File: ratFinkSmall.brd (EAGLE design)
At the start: 82.2 x 80 mm, 30 parts

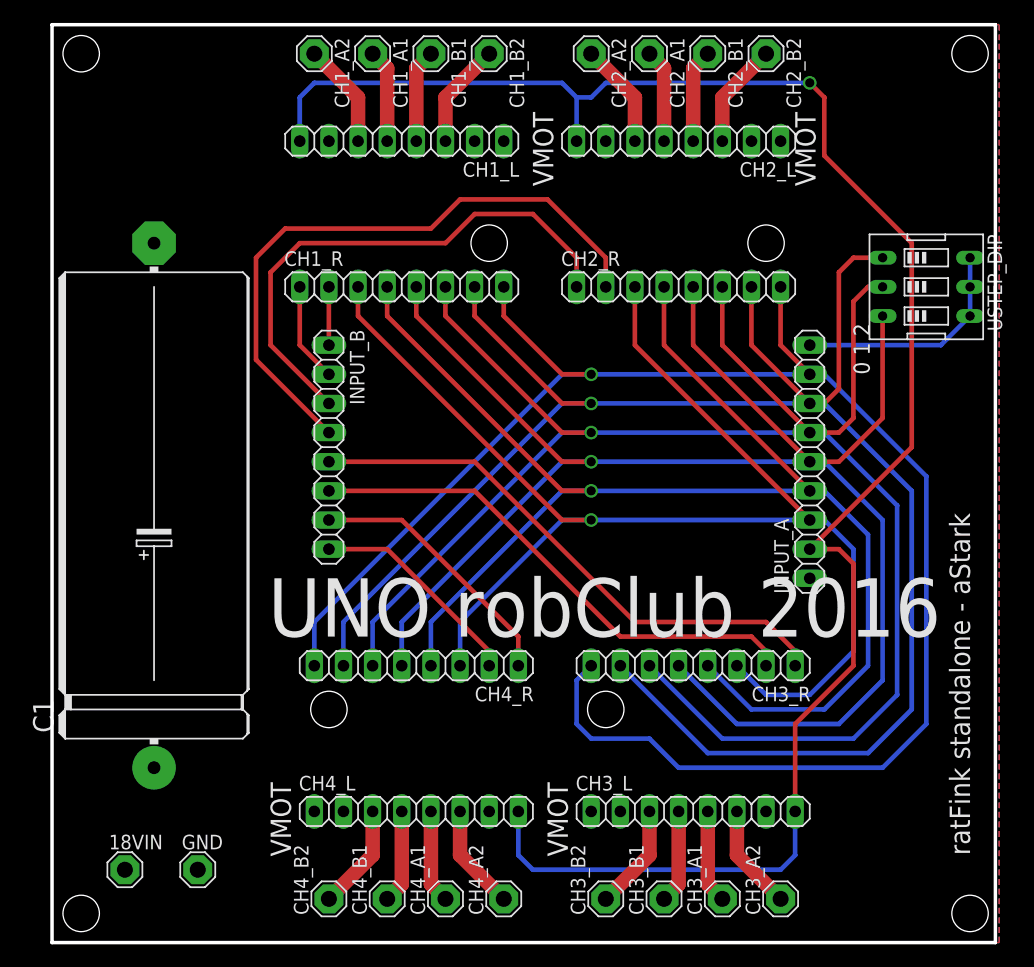
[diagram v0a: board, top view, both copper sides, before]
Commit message: Width decreased by 15mm
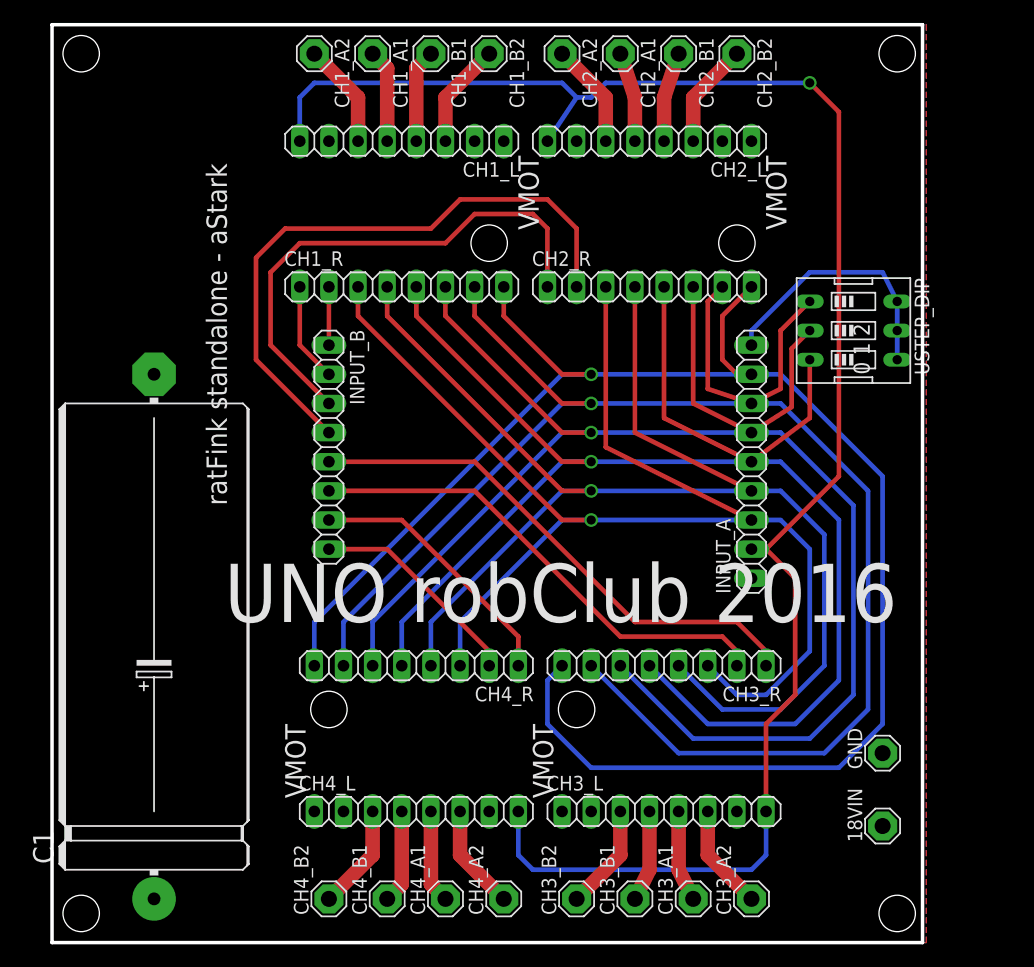
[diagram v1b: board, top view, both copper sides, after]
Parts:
- moved 18VIN 66.1 mm to (90.2, 10.2), turned to 90 degrees
- moved GND 60.5 mm to (90.2, 16.5), turned to 90 degrees
- moved C1 11.4 mm to (26.7, 26.7)
- moved USTEP_DIP 7.41 mm to (87.6, 53.3)
- moved INPUT_A 5.08 mm to (78.7, 41.9)
- moved CH2_B1 2.54 mm to (72.4, 77.5)
- moved CH2_B2 2.54 mm to (77.5, 77.5)
- moved CH2_L 2.54 mm to (69.8, 69.8)
- moved CH2_R 2.54 mm to (69.8, 57.1)
- moved CH3_A1 2.54 mm to (73.7, 3.81)
- moved CH3_A2 2.54 mm to (78.7, 3.81)
- moved CH3_B1 2.54 mm to (68.6, 3.81)
- moved CH3_B2 2.54 mm to (63.5, 3.81)
- moved CH2_A2 2.54 mm to (62.2, 77.5)
- moved CH2_A1 2.54 mm to (67.3, 77.5)
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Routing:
- net M1: track 154.2 -> 143.0 mm
- net M2: track 148.4 -> 138.4 mm
- net M0: track 159.3 -> 149.3 mm
- net FLT: track 162.5 -> 156.5 mm
- net RST: track 126.5 -> 122.4 mm
- net SLP: track 121.4 -> 117.8 mm
- net EN: track 151.5 -> 148.3 mm
- net 5VIN: track 20.1 -> 22.7 mm
- net N$8: track 48.7 -> 46.2 mm
- net N$9: track 45.2 -> 42.6 mm
- net N$4: track 55.1 -> 54.0 mm
- net N$1: track 46.4 -> 45.4 mm
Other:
- board size 82.2 x 80 mm -> 75.9 x 80 mm
